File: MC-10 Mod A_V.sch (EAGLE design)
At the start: 28 parts, among them K1 PG203J, Q1 BC327, Q2 BC338, U1 MC1372, X1 3.579545

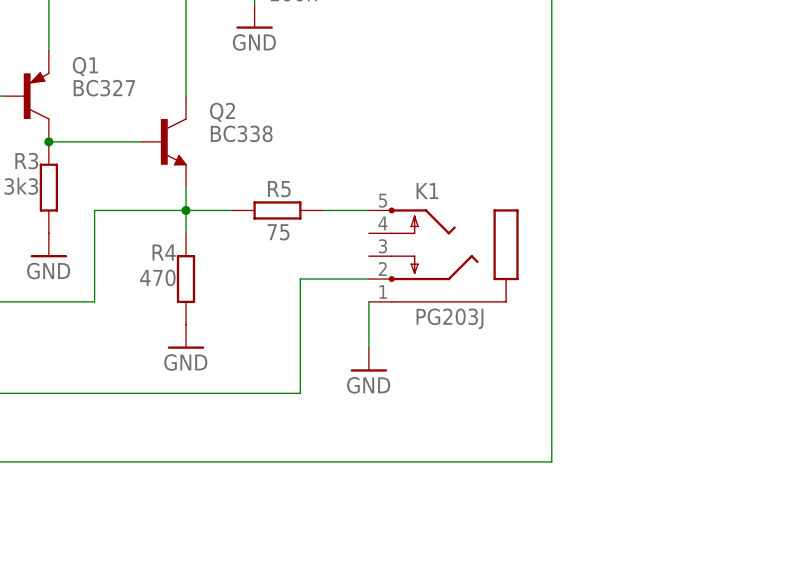
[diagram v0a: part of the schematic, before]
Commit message: Updated PCB for AV Mod
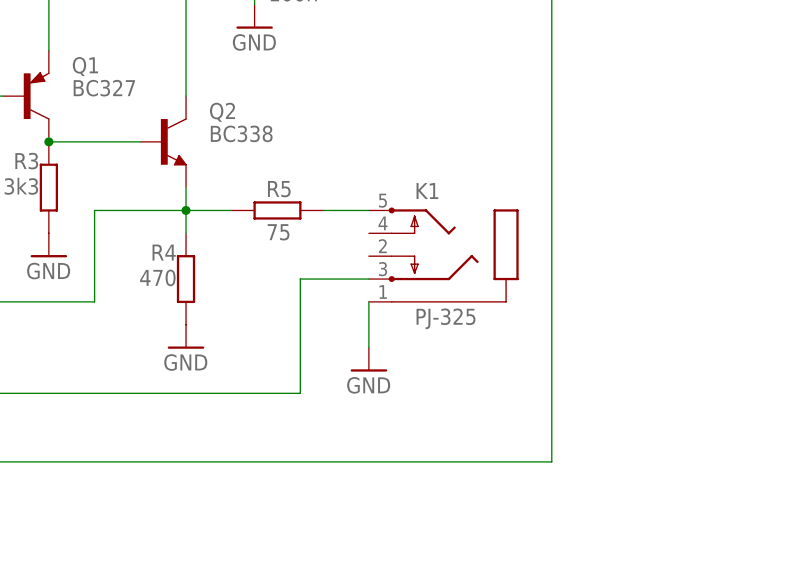
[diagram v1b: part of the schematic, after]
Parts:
- K1: value PG203J -> PJ-325; device con-hirschmann:PG203J -> AudioJack:PJ-325
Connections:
- net N$5: now also K1.3; no longer K1.2
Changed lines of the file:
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@@
 <part name="GND1" library="supply1" deviceset="GND" device=""/>
 <part name="R5" library="rcl" deviceset="R-EU_" device="0204/7" value="75"/>
-<part name="K1" library="con-hirschmann" deviceset="PG203J" device=""/>
 <part name="R7" library="rcl" deviceset="R-EU_" device="0204/7" value="68k"/>
 <part name="R8" library="rcl" deviceset="R-EU_" device="0204/7" value="15k"/>
@@
 <part name="L1" library="inductor-neosid" deviceset="BS" device="75" value="47uH"/>
 <part name="FRAME1" library="frames" deviceset="A4L-LOC" device=""/>
+<part name="K1" library="AudioJack" deviceset="PJ-325" device=""/>
 </parts>
 <sheets>
@@
 <attribute name="VALUE" x="184.15" y="70.358" size="1.778" layer="96"/>
 </instance>
-<instance part="K1" gate="1" x="208.28" y="71.12"/>
 <instance part="R7" gate="G$1" x="86.36" y="76.2" smashed="yes" rot="R180">
 <attribute name="NAME" x="84.836" y="79.9846" size="1.778" layer="95"/>
@@
 <instance part="L1" gate="G$1" x="203.2" y="106.68"/>
 <instance part="FRAME1" gate="G$1" x="0" y="0"/>
+<instance part="K1" gate="G$1" x="208.28" y="71.12"/>
 </instances>
 <busses>
@@
 </segment>
 <segment>
-<pinref part="K1" gate="1" pin="1"/>
 <pinref part="GND21" gate="1" pin="GND"/>
 <wire x1="195.58" y1="58.42" x2="195.58" y2="63.5" width="0.1524" layer="91"/>
+<pinref part="K1" gate="G$1" pin="1"/>
 </segment>
 <segment>
@@
 <segment>
 <pinref part="R5" gate="G$1" pin="2"/>
-<pinref part="K1" gate="1" pin="5"/>
 <wire x1="195.58" y1="73.66" x2="190.5" y2="73.66" width="0.1524" layer="91"/>
+<pinref part="K1" gate="G$1" pin="5"/>
 </segment>
 </net>
@@
 <wire x1="119.38" y1="53.34" x2="187.96" y2="53.34" width="0.1524" layer="91"/>
 <wire x1="187.96" y1="53.34" x2="187.96" y2="66.04" width="0.1524" layer="91"/>
-<pinref part="K1" gate="1" pin="2"/>
-<wire x1="187.96" y1="66.04" x2="195.58" y2="66.04" width="0.1524" layer="91"/>
-</segment>
-</net>
+<pinref part="K1" gate="G$1" pin="3"/>
+<wire x1="195.58" y1="66.04" x2="187.96" y2="66.04" width="0.1524" layer="91"/>
+</segment>
+</net>

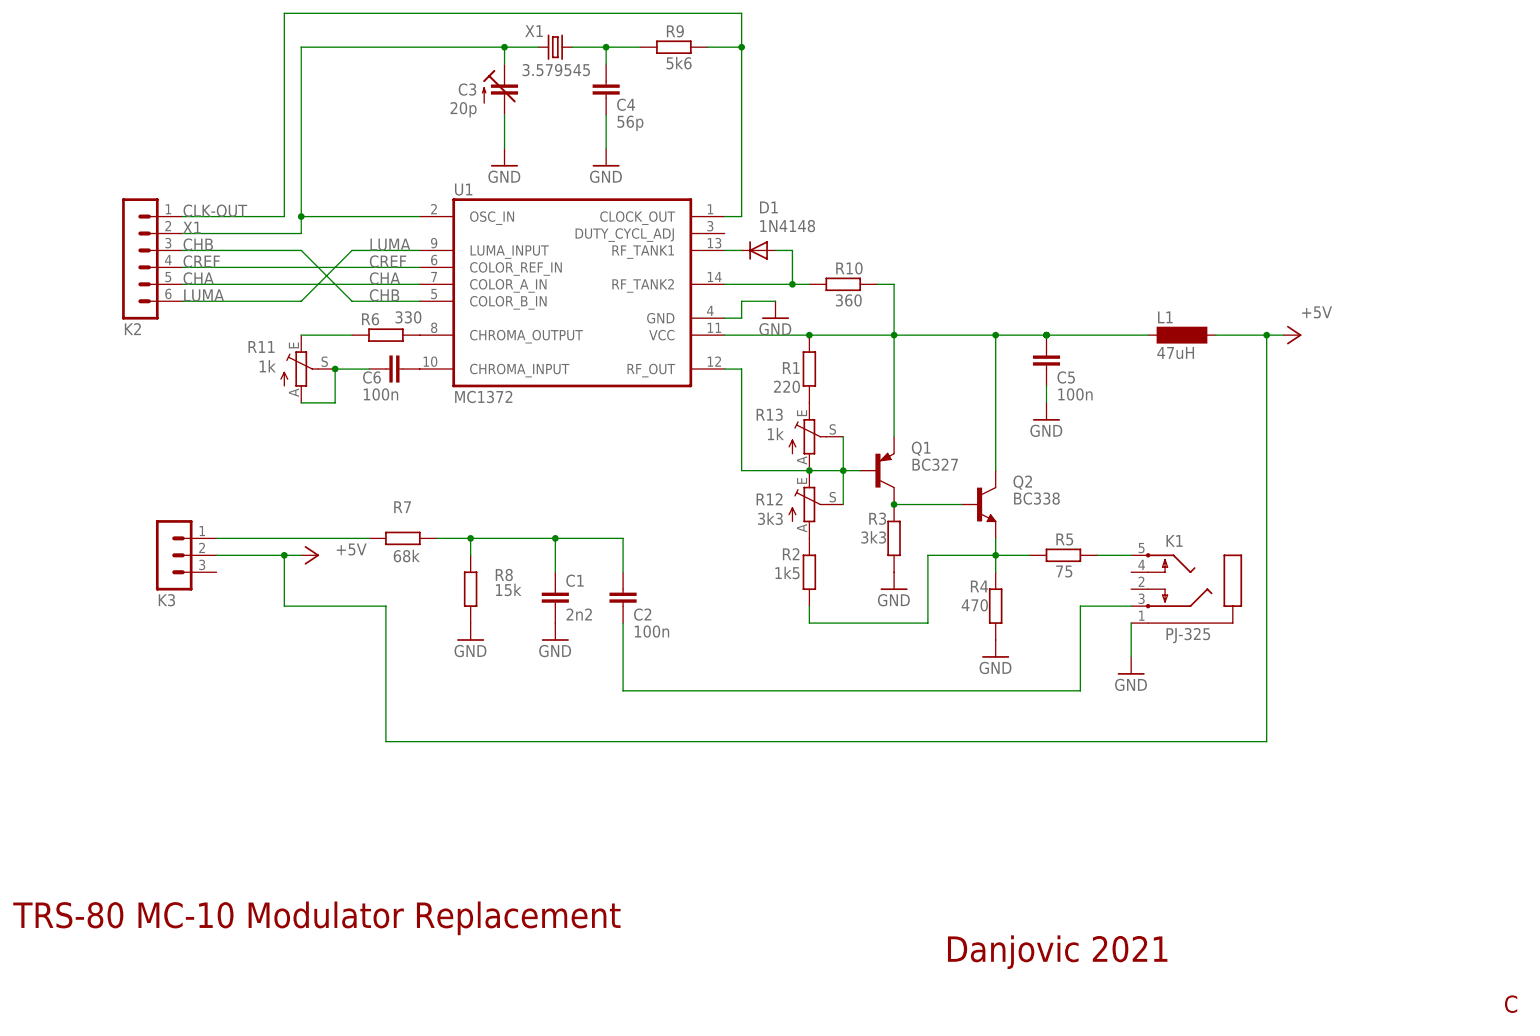
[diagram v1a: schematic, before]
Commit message: Updated AV mod Schematics and PCB
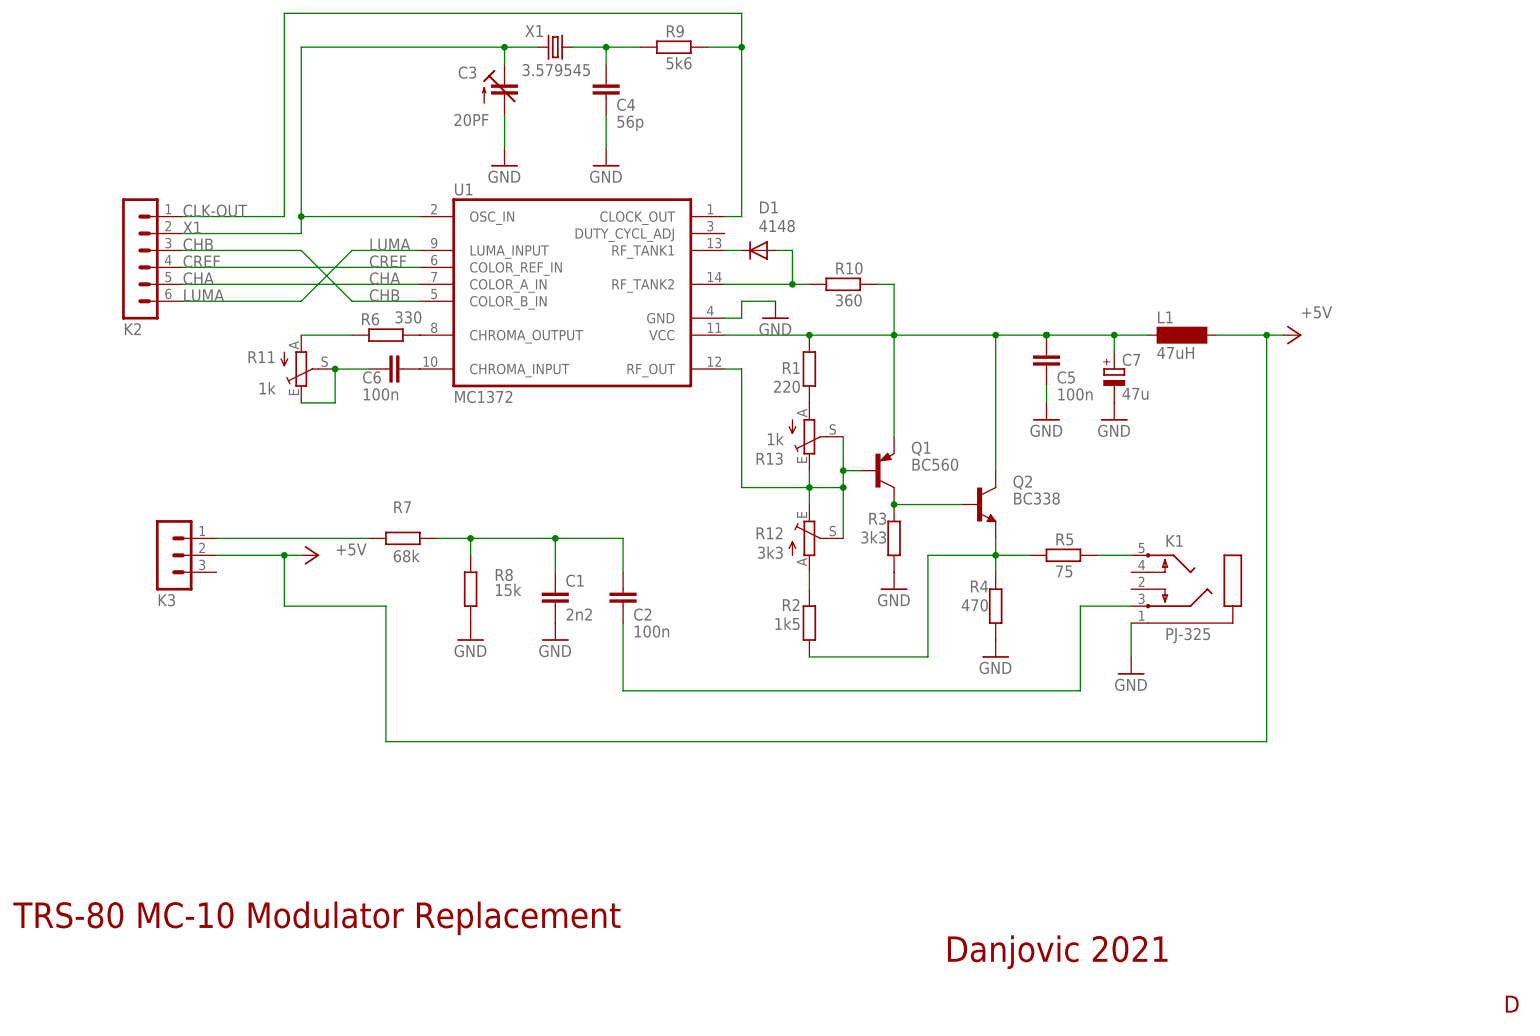
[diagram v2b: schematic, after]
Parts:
- added C7: 47u, rcl:CPOL-EUE2.5-5
- C3: value 20p -> 20PF; device c-trimm:C-TRIMM3008 -> rcl:C-TRIMM3050.504
- D1: value 1N4148 -> 4148
- Q1: value BC327 -> BC560
- R11, R12, R13: device pot:TRIM_EU-B25P -> pot:TRIM_EU-RS3
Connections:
- net N$2 renamed VID-OUT
- net N$5 renamed AUD-OUT
- removed net N$15: R11.E, R6.1
- new net N$6: R11.A, R6.1
- net GND: now also C7.-
- net N$10: now also R13.A; no longer R13.E
- net N$11: now also R11.E; no longer R11.A
- net N$7: now also R13.E; no longer R13.A
- net VCC: now also C7.+
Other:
- note added: "D"
- note removed: "C"
- moved on the sheet: R11, R12, R13, R2
